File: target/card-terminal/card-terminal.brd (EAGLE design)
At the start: 77 x 70.8 mm, 33 parts, among them IC1 74S113D, Q1 16 MHz, Q2 BSS123, Q3 BSS123, Q4 BSS123, Q5 BSS123, Q6 BSS123, X2 5036-008-210-862

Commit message: fixes for card-terminal hardware
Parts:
- moved R2 0.22 mm to (45.9, 42.4)
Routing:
- net GND: track 324.0 -> 322.1 mm
- net RTS: track 79.1 -> 77.4 mm

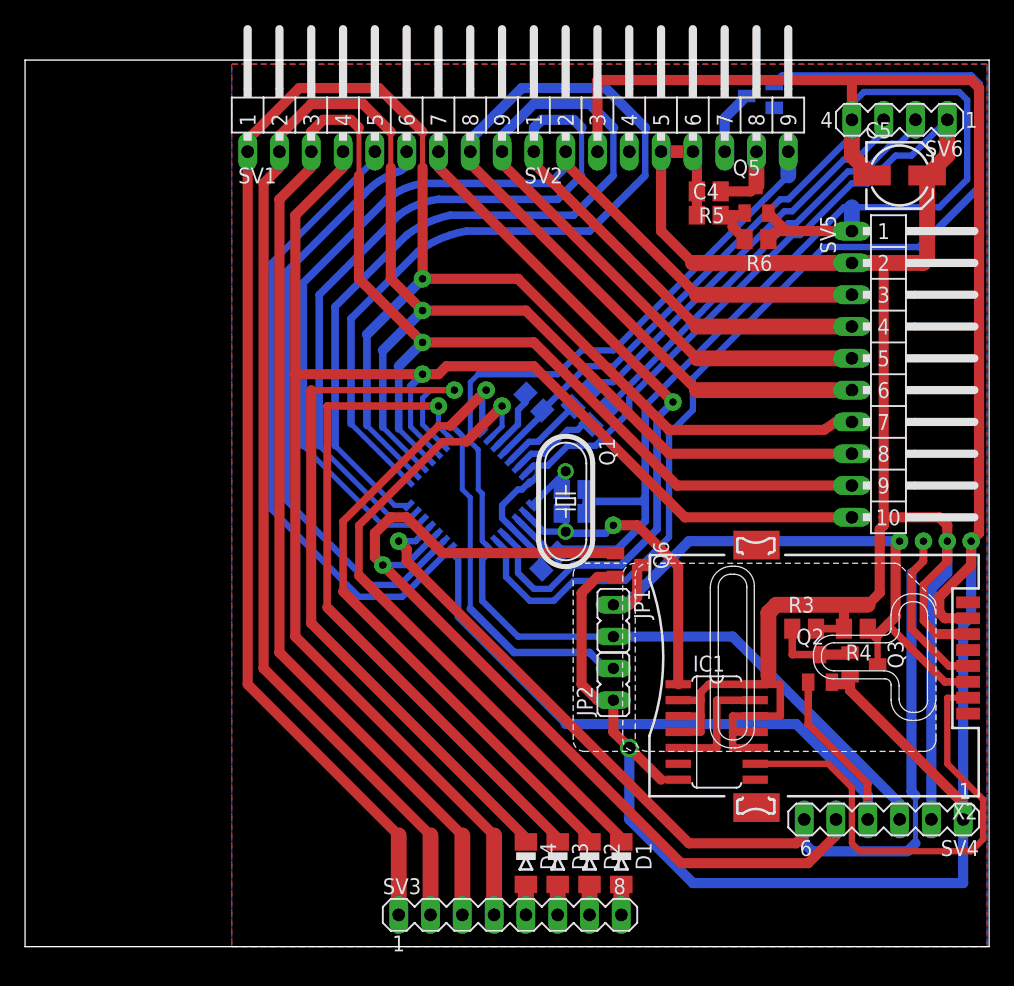
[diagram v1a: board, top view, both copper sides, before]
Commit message: card-terminal: hardware fixes
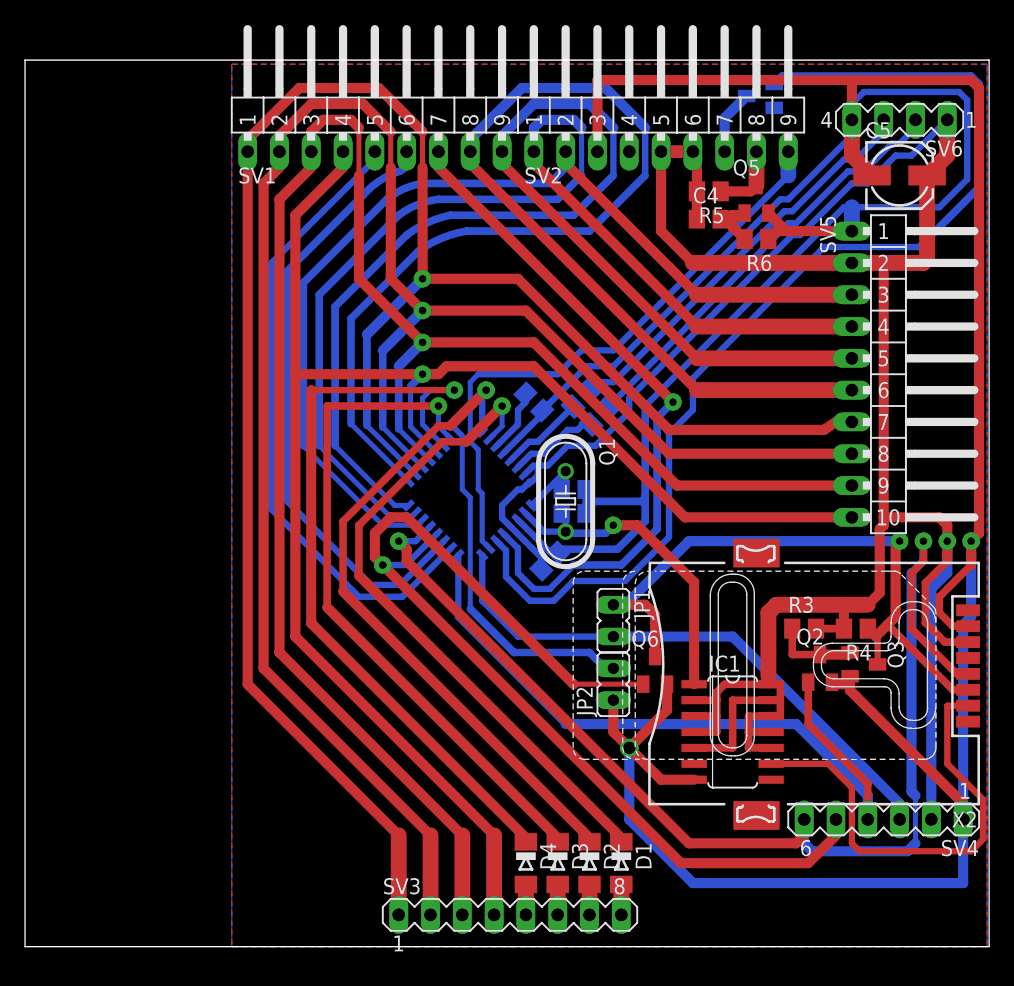
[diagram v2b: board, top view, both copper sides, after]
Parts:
- moved Q6 8.66 mm to (50.3, 22.1), turned to 0 degrees
- moved IC1 1.27 mm to (56.5, 17.1)
- moved X2 0.64 mm to (58.4, 21.0)
- moved C4 0.32 mm to (54.6, 58.1)
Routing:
- net RTS: track 77.4 -> 83.9 mm
- net GND: track 322.1 -> 316.4 mm
- net RX_TX: track 50.1 -> 52.3 mm
- net VCC: track 219.7 -> 217.6 mm
- net CLK: track 38.2 -> 36.3 mm
- net XTAL2: track 25.6 -> 26.1 mm

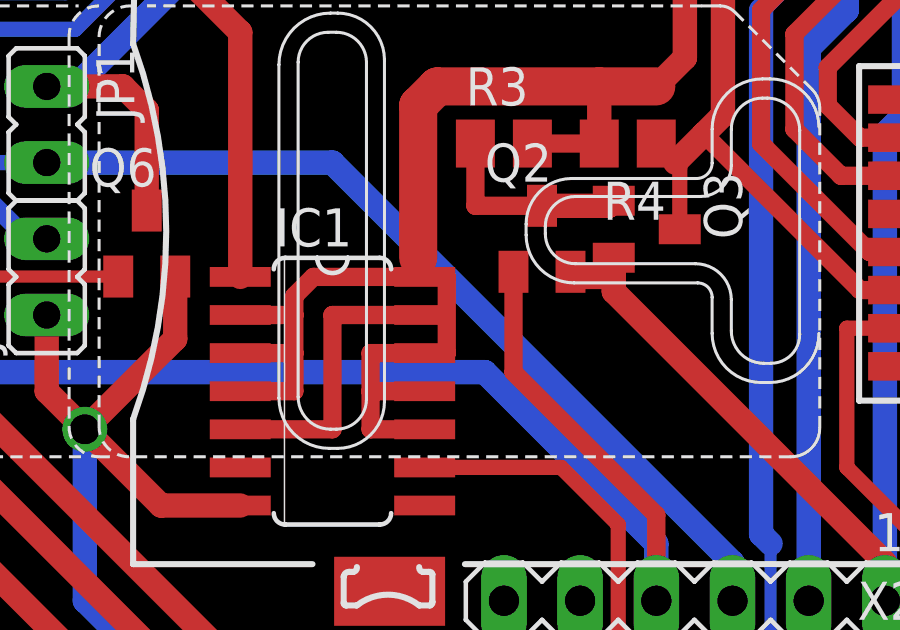
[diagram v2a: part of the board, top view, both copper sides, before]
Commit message: card-terminal: hardware fixes
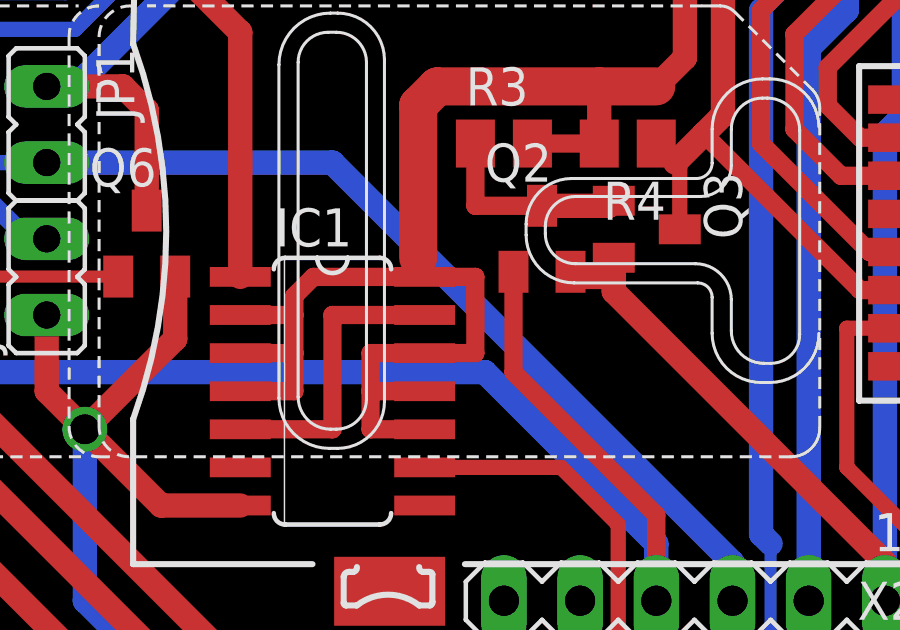
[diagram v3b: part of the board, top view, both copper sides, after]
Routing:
- net VCC: track 217.6 -> 219.5 mm
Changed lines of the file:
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@@
 <wire x1="53.66" y1="60.325" x2="53.66" y2="58.1025" width="0.8128" layer="1"/>
 <wire x1="59.5884" y1="20.955" x2="59.69" y2="20.955" width="0.6096" layer="1"/>
-<wire x1="59.69" y1="20.955" x2="60.325" y2="20.955" width="0.6096" layer="1"/>
-<wire x1="60.325" y1="20.955" x2="60.325" y2="18.415" width="0.6096" layer="1"/>
-<wire x1="60.325" y1="18.415" x2="59.5884" y2="18.415" width="0.6096" layer="1"/>
+<wire x1="59.69" y1="20.955" x2="61.2775" y2="20.955" width="0.6096" layer="1"/>
+<wire x1="61.2775" y1="20.955" x2="61.2775" y2="18.415" width="0.6096" layer="1"/>
+<wire x1="61.2775" y1="18.415" x2="59.5884" y2="18.415" width="0.6096" layer="1"/>
 <wire x1="60.0075" y1="27.305" x2="59.3725" y2="26.67" width="1.27" layer="1"/>
 <wire x1="59.3725" y1="26.67" x2="59.3725" y2="21.59" width="1.27" layer="1"/>
